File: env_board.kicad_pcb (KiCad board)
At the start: 2 copper layers, 20.7 x 19.2 mm, 23 parts, among them J1 CONN_01X07, J2 BATT_CONN, P1 USB_OTG, Q1 Q_NMOS_GSD, Q2 Q_PMOS_GSD, U1 RFD77101, U2 ENS210, U3 CCS811, U4 AP2204K-3.0, U5 MCP73811T-420I-OT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

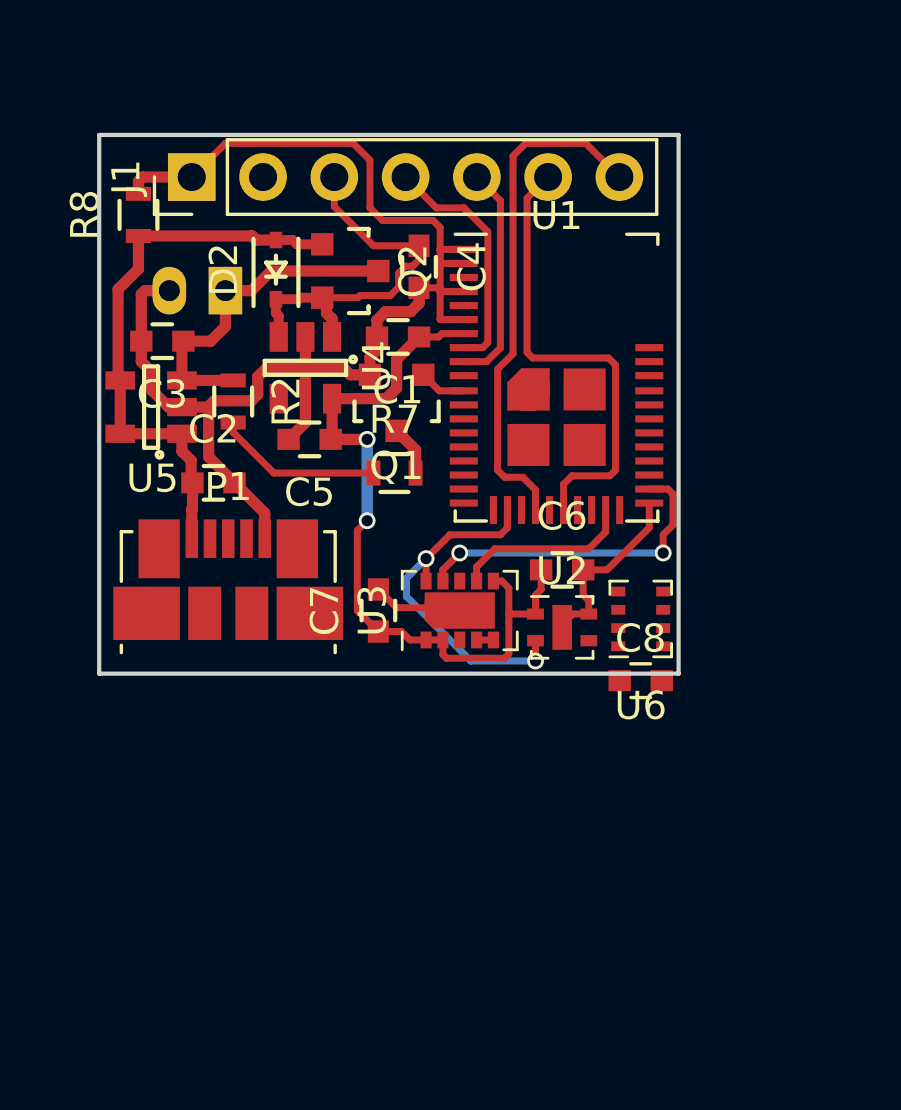
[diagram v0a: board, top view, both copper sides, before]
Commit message: changes to use nRF52840 instead of simblee
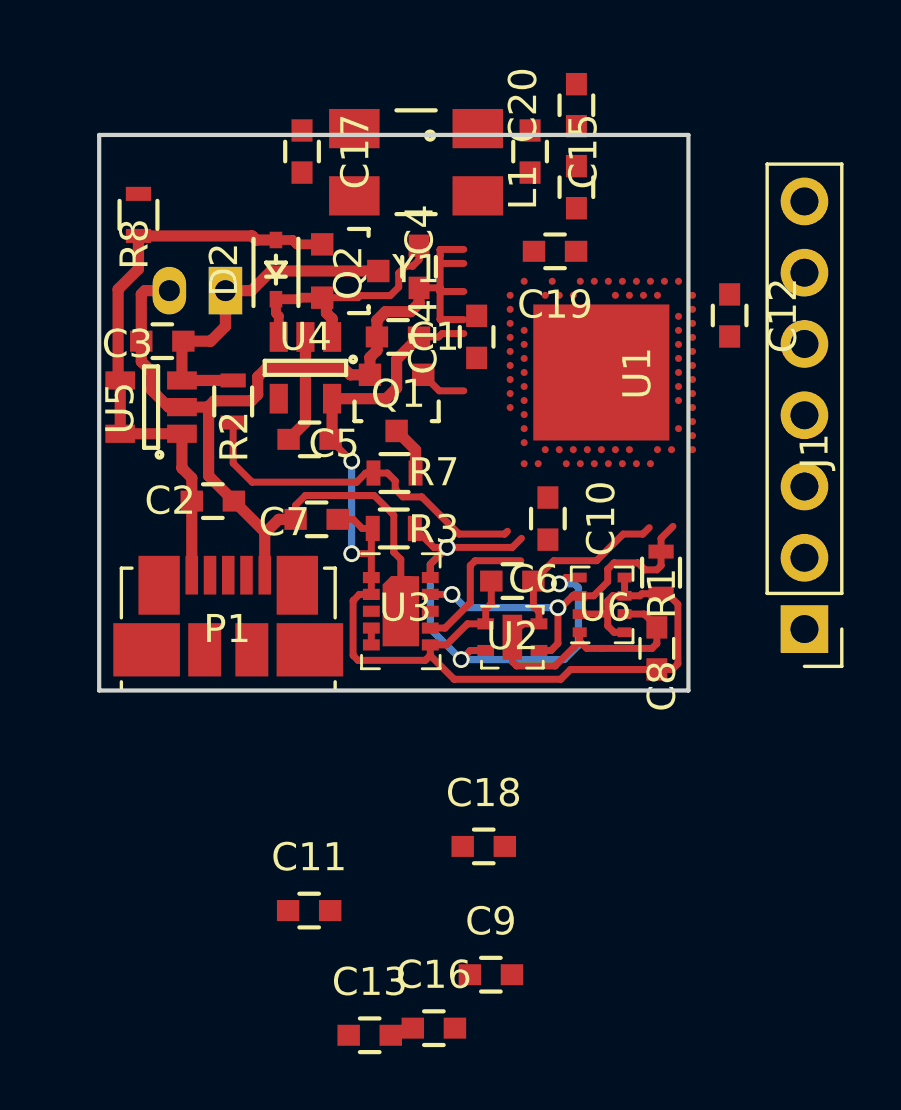
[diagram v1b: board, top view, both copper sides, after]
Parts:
- added C10: 1u, Capacitors_SMD:C_0603, F.Cu at (164.2, 111.2)
- added C11: 100n, Capacitors_SMD:C_0603, F.Cu at (155.7, 125.1)
- added C12: 100n, Capacitors_SMD:C_0603, F.Cu at (170.7, 103.9)
- added C13: 4.7u, Capacitors_SMD:C_0603, F.Cu at (157.8, 129.6)
- added C14: 1u, Capacitors_SMD:C_0603, F.Cu at (161.7, 104.7)
- added C15: 12p, Capacitors_SMD:C_0603, F.Cu at (163.6, 98.1)
- added C16: 100p, Capacitors_SMD:C_0603, F.Cu at (160.1, 129.3)
- added C17: 12p, Capacitors_SMD:C_0603, F.Cu at (155.4, 98.1)
- added C18: 100n, Capacitors_SMD:C_0603, F.Cu at (161.9, 122.9)
- added C19: 0.8p, Capacitors_SMD:C_0603, F.Cu at (164.4, 101.6)
- added C20: 0.5p, Capacitors_SMD:C_0603, F.Cu at (165.2, 96.4)
- added C9: 100n, Capacitors_SMD:C_0603, F.Cu at (162.2, 127.4)
- added L1: 33nH, Capacitors_SMD:C_0603, F.Cu at (165.2, 99.4)
- added R1: 10k, Resistors_SMD:R_0603, F.Cu at (168.2, 113.1)
- added R3: 10k, Resistors_SMD:R_0603, F.Cu at (158.7, 111.5)
- added Y1: 32MHz, Crystals:Crystal_SMD_0603_4Pads, F.Cu at (159.5, 98.5)
- U1: value RFD77101 -> nRF52840; footprint kicad-RF_Modules:RFDigital_RFD77101 -> Package_DFN_QFN:Nordic_AQFN-73-1EP_7x7mm_P0.5mm
- moved J1 27.1 mm to (173.3, 115.1), turned to 180 degrees
- moved C7 3.92 mm to (155.9, 111.2), turned to 180 degrees
- moved U3 2.10 mm to (158.9, 114.5), turned to 0 degrees
- moved C6 1.82 mm to (162.9, 113.4)
- moved U2 1.81 mm to (162.9, 115.4)
- moved U1 1.61 mm to (166.1, 106.0), turned to 90 degrees
- moved U6 1.46 mm to (166.1, 114.2)
- moved P1 1.30 mm to (152.8, 115.8)
- moved C8 1.29 mm to (168.1, 115.8), turned to 90 degrees
- moved C2 0.65 mm to (152.2, 110.5)
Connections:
- C8 pad 1: Net-(C8-Pad1) -> VDD
- C8 pad 2: Net-(C8-Pad2) -> GND
- J1 pad 2: Net-(J1-Pad2) -> (no net)
- J1 pad 6: /GPIO0 -> (no net)
- J1 pad 7: /GPIO1 -> (no net)
- P1 pad 2: Net-(P1-Pad2) -> (no net)
- P1 pad 3: Net-(P1-Pad3) -> (no net)
- P1 pad 4: Net-(P1-Pad4) -> (no net)
- Q1 pad 1: /BATT_V_EN -> (no net)
- R2 pad 2: /BATT_V -> /PowerMgmt/BATT_V
- R7 pad 1: /BATT_V -> /PowerMgmt/BATT_V
- U3 pad 3: /CCS_INT -> (no net)
- U3 pad 7: /CCS_WAKE -> (no net)
- U3 pad 8: Net-(U3-Pad8) -> (no net)
- U4 pad 4: Net-(U4-Pad4) -> (no net)
- U6 pad 1: Net-(C8-Pad2) -> GND
- U6 pad 2: Net-(C8-Pad1) -> VDD
- U6 pad 5: Net-(C8-Pad1) -> VDD
- U6 pad 6: Net-(C8-Pad1) -> VDD
- U6 pad 7: Net-(C8-Pad2) -> GND
- U6 pad 8: Net-(C8-Pad1) -> VDD
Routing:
- net /GPIO1: track 18.3 -> 0.00 mm
- net /GPIO0: track 16.6 -> 0.00 mm
- net VDD: track 27.6 -> 44.2 mm
- net /PowerMgmt/BATT_V: track 0.00 -> 12.9 mm
- net /SWDIO/RESET: track 8.62 -> 0.00 mm
- net /SWDCLK: track 7.94 -> 0.00 mm
- net (no net): track 0.00 -> 6.68 mm
- net /SCL: track 12.7 -> 19.3 mm, vias 2 -> 3
- net /CCS_WAKE: track 6.40 -> 0.00 mm
- net /BATT_V: track 5.95 -> 0.00 mm
- net VBUS: track 14.1 -> 9.42 mm
- net GND: track 59.2 -> 61.9 mm
- net /SDA: track 11.7 -> 13.4 mm
- net /BATT_V_EN: track 1.68 -> 0.00 mm
- net Net-(C2-Pad1): track 20.5 -> 21.8 mm
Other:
- board size 20.7 x 19.2 mm -> 21 x 19.8 mm
